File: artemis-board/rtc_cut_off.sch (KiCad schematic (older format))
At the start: 17 parts, among them Q1 2N7002, Q10 AO3401A, Q11 2N7002, Q3 2N7002, U7 PCF8563T, U9 TCA6408A, Y2 32.768KHz

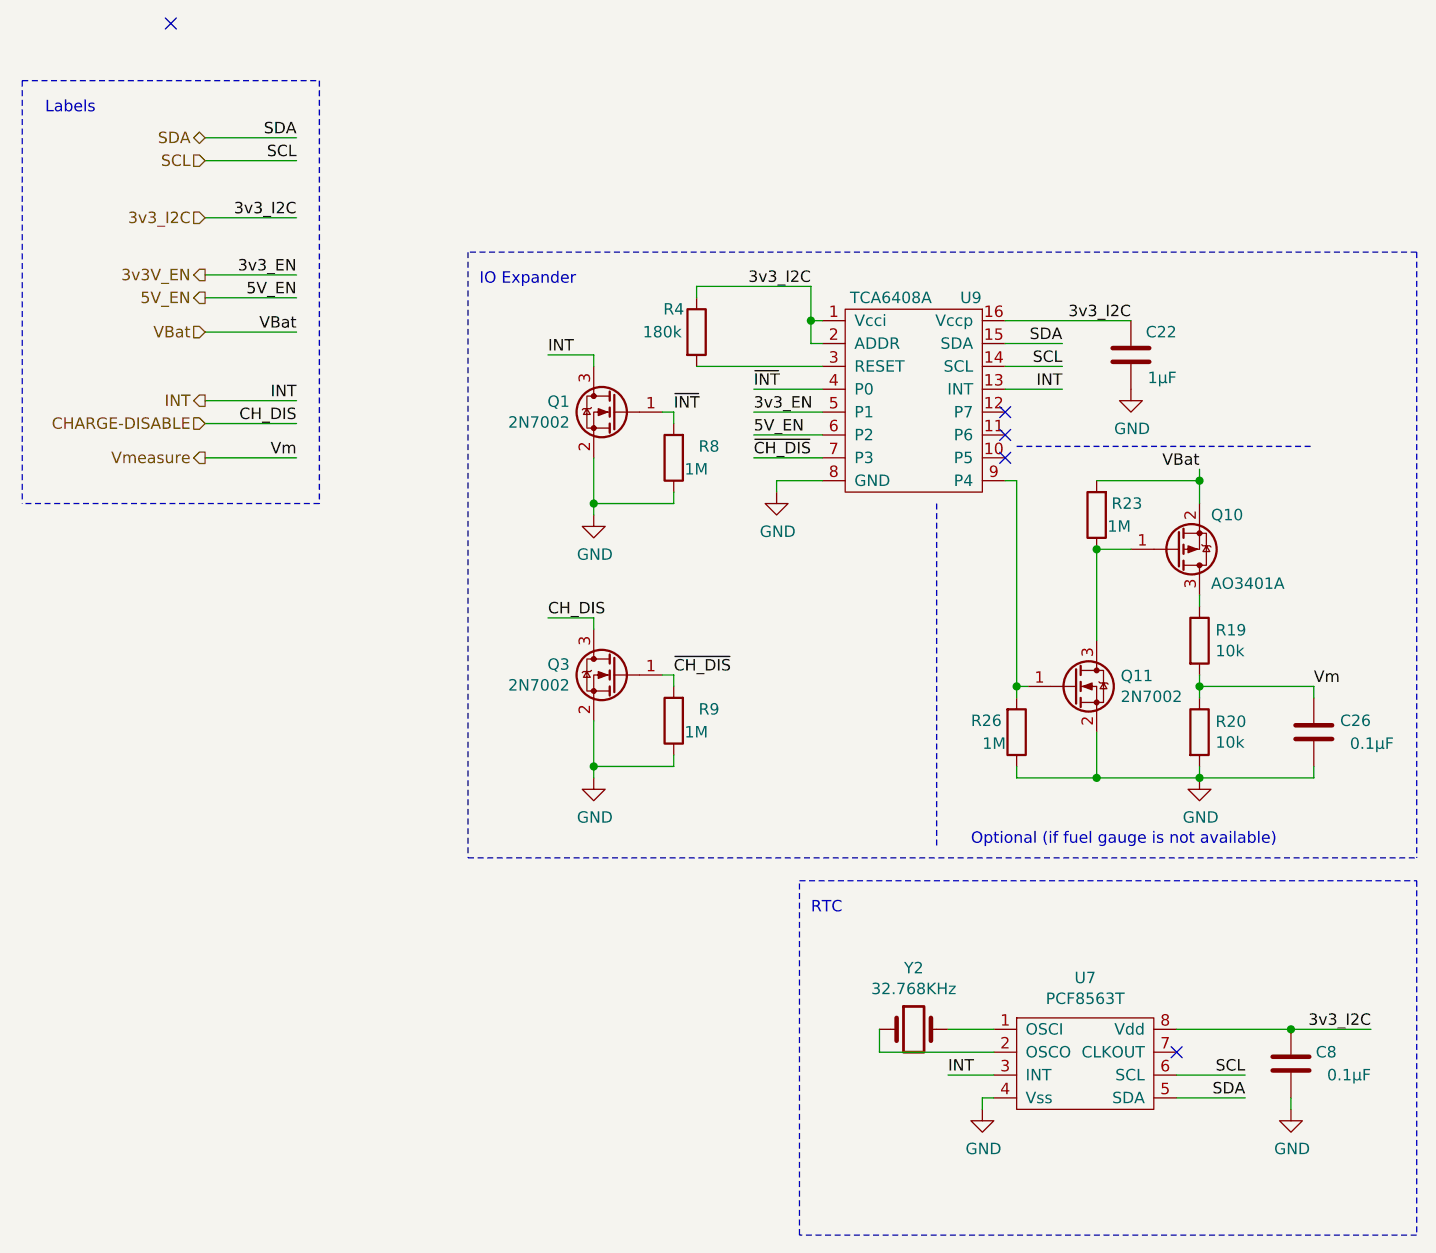
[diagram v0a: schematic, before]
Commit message: added PCA9557 and swapped IO expander for it
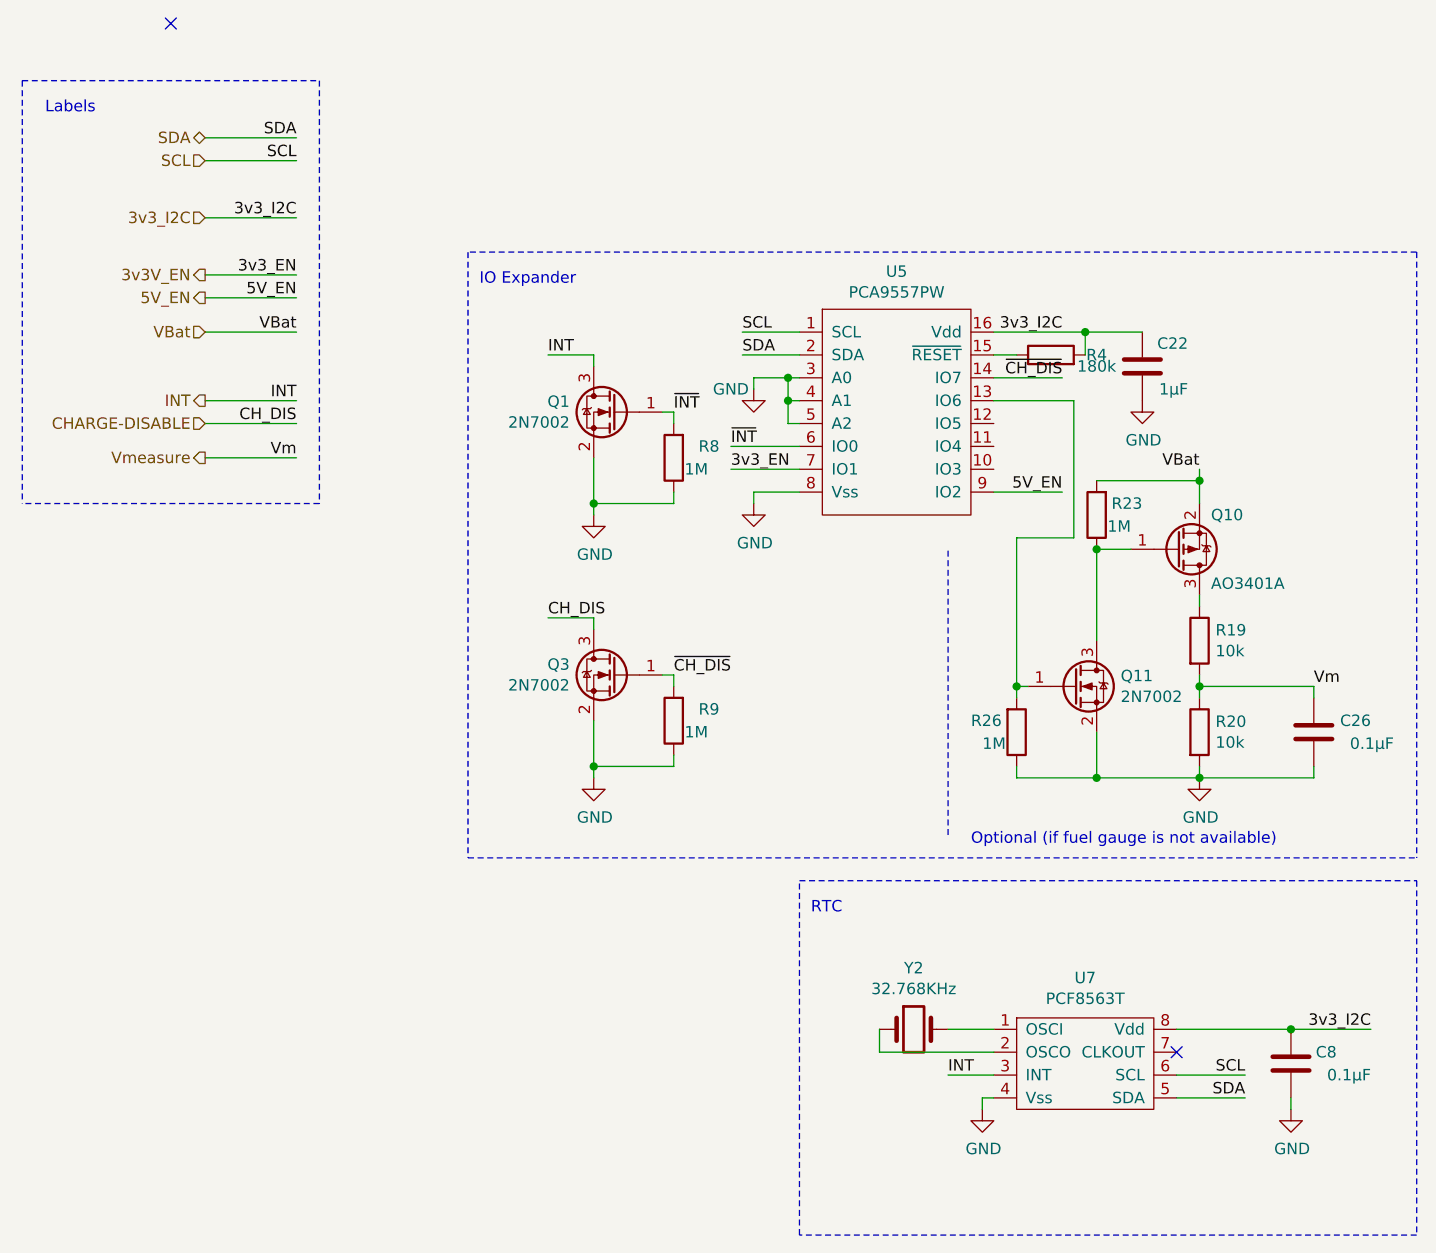
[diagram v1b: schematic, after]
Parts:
- removed U9: TCA6408A, Package_SO:TSSOP-16_4.4x5mm_P0.65mm, symbol TCA6408APWR:TCA6408A
- added U5: PCA9557PW, Package_SO:TSSOP-16_4.4x5mm_P0.65mm, symbol PCA9557:PCA9557PW
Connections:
- net 3v3V_EN: now also U5.7 (IO1)
- net 3v3_I2C: now also R4.2, U5.16 (Vdd); no longer R4.1
- net 5V_EN: now also U5.9 (IO2)
- net GND: now also U5.3 (A0), U5.4 (A1), U5.5 (A2), U5.8 (Vss)
- net SCL: now also U5.1 (SCL)
- net SDA: now also U5.2 (SDA)
- net ~CH_DIS: now also U5.14 (IO7)
- net ~INT: now also U5.6 (IO0)
- net at Q11.1 (G), R26.2: now also U5.13 (IO6)
- new net: R4.1, U5.15 (~RESET)
- no-connect marks 5 -> 2
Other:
- moved on the sheet: C22, R4
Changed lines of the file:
@@
 	4300 4850 4800 4850
 NoConn ~ 5600 4850
-$Comp
-L TCA6408APWR:TCA6408A U9
-U 1 1 5F8103C2
-P 4450 1800
-F 0 "U9" H 4700 2050 50  0000 C CNN
-F 1 "TCA6408A" H 4350 2050 50  0000 C CNN
-F 2 "Package_SO:TSSOP-16_4.4x5mm_P0.65mm" H 4500 2300 50  0001 C CNN
-F 3 "https://www.ti.com/lit/ds/symlink/tca6408a.pdf?ts=1602171918658&ref_url=https%253A%252F%252Fwww.ti.com%252Fproduct%252FTCA6408A" H 4700 2050 50  0001 C CNN
-F 4 "C206177" H 4700 2450 50  0001 C CNN "LCSC"
-	1    4450 1800
-	1    0    0    -1
-$EndComp
 Text HLabel 1350 1200 0    50   Input ~ 0
 3v3_I2C
-Wire Wire Line
-	4050 1650 4000 1650
 $Comp
 L power:GND #PWR0109
@@
 Wire Wire Line
 	2850 1800 3050 1800
-Text Label 5100 1950 2    50   ~ 0
-INT
-Wire Wire Line
-	4850 1950 5100 1950
 Wire Wire Line
 	1350 2000 1750 2000
@@
 Wire Wire Line
 	1350 850  1750 850
-Text Label 5100 1750 2    50   ~ 0
-SDA
-Text Label 5100 1850 2    50   ~ 0
-SCL
-Wire Wire Line
-	4850 1750 5100 1750
-Wire Wire Line
-	4850 1850 5100 1850
 Wire Wire Line
 	6100 4750 6450 4750
@@
 Wire Notes Line
 	1850 2450 550  2450
-Text Label 3750 2050 0    50   ~ 0
+Text Label 3650 2300 0    50   ~ 0
 3v3_EN
-Text Label 3750 2150 0    50   ~ 0
+Text Label 5100 2400 2    50   ~ 0
 5V_EN
-Text Label 3750 2250 0    50   ~ 0
+Text Label 5100 1900 2    50   ~ 0
 ~CH_DIS
-$Comp
-L Device:R R4
-U 1 1 5FC6F3D4
-P 3500 1700
-F 0 "R4" H 3400 1800 50  0000 C CNN
-F 1 "180k" H 3350 1700 50  0000 C CNN
-F 2 "Resistor_SMD:R_0603_1608Metric_Pad1.05x0.95mm_HandSolder" V 3430 1700 50  0001 C CNN
-F 3 "~" H 3500 1700 50  0001 C CNN
-F 4 "C22827" H 3500 1700 50  0001 C CNN "LCSC"
-	1    3500 1700
-	1    0    0    -1
-$EndComp
-Wire Wire Line
-	4000 1500 4000 1650
-Text Label 4000 1500 2    50   ~ 0
+Text Label 5100 1700 2    50   ~ 0
 3v3_I2C
 Wire Wire Line
@@
 L Device:C C22
 U 1 1 5FC9C8EC
-P 5400 1800
-F 0 "C22" H 5200 1700 50  0000 L CNN
-F 1 "1µF" H 5200 1900 50  0000 L CNN
-F 2 "Capacitor_SMD:C_0603_1608Metric_Pad1.08x0.95mm_HandSolder" H 5438 1650 50  0001 C CNN
-F 3 "~" H 5400 1800 50  0001 C CNN
-F 4 "C15849" H 5400 1800 50  0001 C CNN "LCSC"
-	1    5400 1800
+P 5450 1850
+F 0 "C22" H 5250 1750 50  0000 L CNN
+F 1 "1µF" H 5250 1950 50  0000 L CNN
+F 2 "Capacitor_SMD:C_0603_1608Metric_Pad1.08x0.95mm_HandSolder" H 5488 1700 50  0001 C CNN
+F 3 "~" H 5450 1850 50  0001 C CNN
+F 4 "C15849" H 5450 1850 50  0001 C CNN "LCSC"
+	1    5450 1850
 	-1   0    0    1
 $EndComp
-Wire Wire Line
-	4850 1650 5400 1650
 $Comp
 L power:GND #PWR0110
 U 1 1 5FCA03ED
-P 5400 1950
-F 0 "#PWR0110" H 5400 1700 50  0001 C CNN
-F 1 "GND" H 5405 1777 50  0000 C CNN
-F 2 "" H 5400 1950 50  0001 C CNN
-F 3 "" H 5400 1950 50  0001 C CNN
-	1    5400 1950
+P 5450 2000
+F 0 "#PWR0110" H 5450 1750 50  0001 C CNN
+F 1 "GND" H 5455 1827 50  0000 C CNN
+F 2 "" H 5450 2000 50  0001 C CNN
+F 3 "" H 5450 2000 50  0001 C CNN
+	1    5450 2000
 	1    0    0    -1
 $EndComp
@@
 3v3_I2C
 Wire Wire Line
-	3750 2050 4050 2050
-Wire Wire Line
-	4050 2150 3750 2150
-Wire Wire Line
-	3750 2250 4050 2250
-NoConn ~ 4850 2250
-NoConn ~ 4850 2150
-NoConn ~ 4850 2050
-Wire Wire Line
-	3500 1850 4050 1850
+	3950 2300 3650 2300
+Wire Wire Line
+	4800 2400 5100 2400
+Wire Wire Line
+	5100 1900 4800 1900
 Text HLabel 1350 1700 0    50   Input ~ 0
 VBat
@@
 Wire Wire Line
 	1750 1700 1350 1700
-Wire Wire Line
-	3500 1550 3500 1500
-Wire Wire Line
-	4050 1750 4000 1750
-Wire Wire Line
-	4000 1750 4000 1650
-Connection ~ 4000 1650
-Text Label 3750 1950 0    50   ~ 0
+Text Label 3650 2200 0    50   ~ 0
 ~INT
 Wire Wire Line
-	3750 1950 4050 1950
-Wire Wire Line
-	4050 2350 3850 2350
-Wire Wire Line
-	3850 2350 3850 2400
+	3650 2200 3950 2200
+Wire Wire Line
+	3950 2400 3750 2400
+Wire Wire Line
+	3750 2400 3750 2450
 $Comp
 L power:GND #PWR0111
 U 1 1 60A0ABA2
-P 3850 2400
-F 0 "#PWR0111" H 3850 2150 50  0001 C CNN
-F 1 "GND" H 3855 2227 50  0000 C CNN
-F 2 "" H 3850 2400 50  0001 C CNN
-F 3 "" H 3850 2400 50  0001 C CNN
-	1    3850 2400
+P 3750 2450
+F 0 "#PWR0111" H 3750 2200 50  0001 C CNN
+F 1 "GND" H 3755 2277 50  0000 C CNN
+F 2 "" H 3750 2450 50  0001 C CNN
+F 3 "" H 3750 2450 50  0001 C CNN
+	1    3750 2450
 	1    0    0    -1
 $EndComp
@@
 Text Notes 4700 3950 0    50   ~ 0
 Optional (if fuel gauge is not available)
-Wire Notes Line
-	4550 2450 4550 3950
-Wire Notes Line
-	4900 2200 6200 2200
 Connection ~ 5700 2350
 Wire Wire Line
@@
 Wire Wire Line
 	6200 3650 5700 3650
-Wire Wire Line
-	4900 3250 4900 2350
-Wire Wire Line
-	4900 2350 4850 2350
+Wire Notes Line
+	6650 1350 2500 1350
+Wire Notes Line
+	2500 4000 6650 4000
+Wire Notes Line
+	2500 1350 2500 4000
+$Comp
+L PCA9557:PCA9557PW U5
+U 1 1 60F0D833
+P 4400 1450
+F 0 "U5" H 4375 1465 50  0000 C CNN
+F 1 "PCA9557PW" H 4375 1374 50  0000 C CNN
+F 2 "Package_SO:TSSOP-16_4.4x5mm_P0.65mm" H 4400 1450 50  0001 C CNN
+F 3 "" H 4400 1450 50  0001 C CNN
+F 4 "C141380" H 4400 1450 50  0001 C CNN "LCSC"
+	1    4400 1450
+	1    0    0    -1
+$EndComp
+Text Label 3700 1800 0    50   ~ 0
+SDA
+Text Label 3700 1700 0    50   ~ 0
+SCL
+Wire Wire Line
+	3950 1800 3700 1800
+Wire Wire Line
+	3950 1700 3700 1700
+$Comp
+L Device:R R4
+U 1 1 5FC6F3D4
+P 5050 1800
+F 0 "R4" V 5050 1600 50  0000 C CNN
+F 1 "180k" V 5000 1600 50  0000 C CNN
+F 2 "Resistor_SMD:R_0603_1608Metric_Pad1.05x0.95mm_HandSolder" V 4980 1800 50  0001 C CNN
+F 3 "~" H 5050 1800 50  0001 C CNN
+F 4 "C22827" H 5050 1800 50  0001 C CNN "LCSC"
+	1    5050 1800
+	0    -1   -1   0
+$EndComp
+Wire Wire Line
+	4800 1800 4900 1800
+Wire Wire Line
+	5200 1700 5200 1800
+Wire Wire Line
+	4800 1700 5200 1700
+Wire Wire Line
+	5450 1700 5200 1700
+Connection ~ 5200 1700
+Wire Notes Line
+	4600 3900 4600 2650
+Wire Wire Line
+	4900 3250 4900 2600
+Wire Wire Line
+	4900 2600 5150 2600
 Connection ~ 4900 3250
-Wire Notes Line
-	6650 1350 2500 1350
-Wire Notes Line
-	2500 4000 6650 4000
-Wire Notes Line
-	2500 1350 2500 4000
-Text Label 5400 1650 2    50   ~ 0
-3v3_I2C
-Wire Wire Line
-	4000 1500 3500 1500
+Wire Wire Line
+	3950 2100 3900 2100
+Wire Wire Line
+	3900 2100 3900 2000
+Wire Wire Line
+	3900 2000 3950 2000
+Wire Wire Line
+	3900 2000 3900 1900
+Wire Wire Line
+	3900 1900 3950 1900
+Connection ~ 3900 2000
+Wire Wire Line
+	3750 1900 3750 1950
+$Comp
+L power:GND #PWR0118
+U 1 1 60F58134
+P 3750 1950
+F 0 "#PWR0118" H 3750 1700 50  0001 C CNN
+F 1 "GND" H 3650 1950 50  0000 C CNN
+F 2 "" H 3750 1950 50  0001 C CNN
+F 3 "" H 3750 1950 50  0001 C CNN
+	1    3750 1950
+	1    0    0    -1
+$EndComp
+Wire Wire Line
+	3750 1900 3900 1900
+Connection ~ 3900 1900
+Wire Wire Line
+	4800 2000 5150 2000
+Wire Wire Line
+	5150 2000 5150 2600
 $EndSCHEMATC

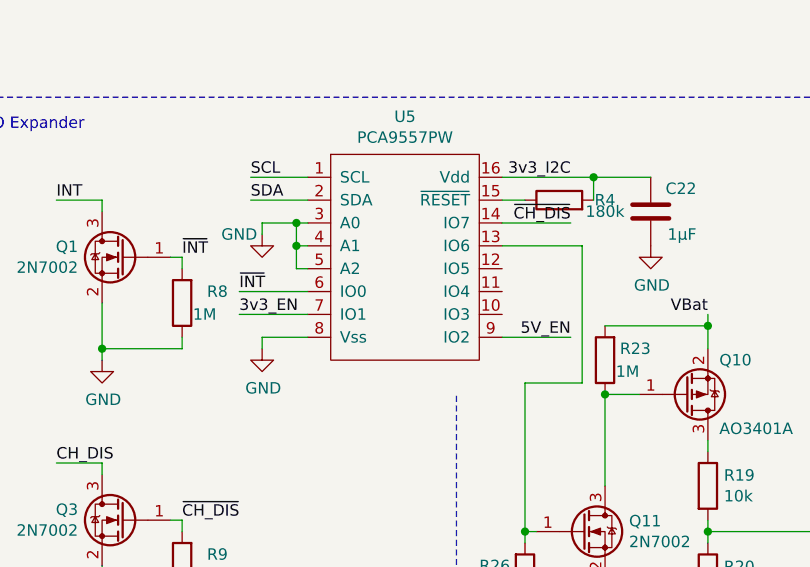
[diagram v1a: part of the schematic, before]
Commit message: added datasheet for pca9557 and connected ~INT to another pin
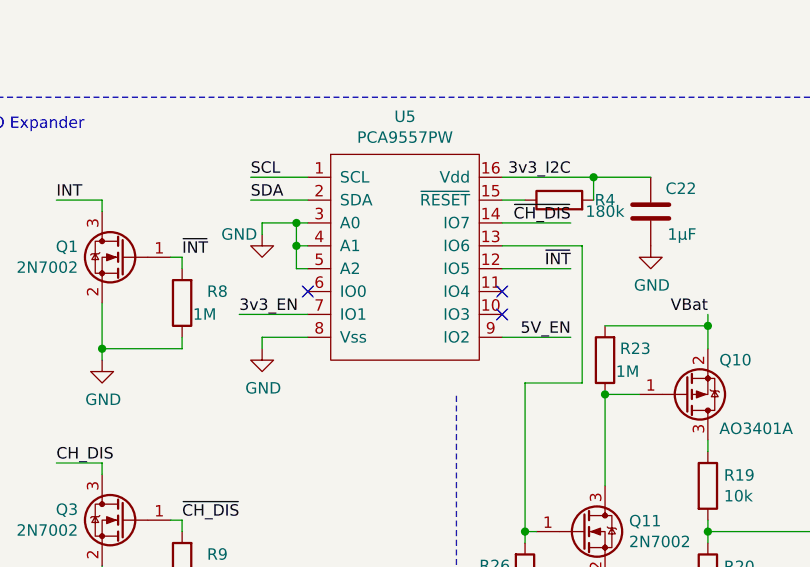
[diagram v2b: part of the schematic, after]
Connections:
- net ~INT: now also U5.12 (IO5); no longer U5.6 (IO0)
- no-connect marks 2 -> 5
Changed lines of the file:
@@
 Wire Wire Line
 	1750 1700 1350 1700
-Text Label 3650 2200 0    50   ~ 0
+Text Label 5100 2100 2    50   ~ 0
 ~INT
 Wire Wire Line
-	3650 2200 3950 2200
+	5100 2100 4800 2100
 Wire Wire Line
 	3950 2400 3750 2400
@@
 F 1 "PCA9557PW" H 4375 1374 50  0000 C CNN
 F 2 "Package_SO:TSSOP-16_4.4x5mm_P0.65mm" H 4400 1450 50  0001 C CNN
-F 3 "" H 4400 1450 50  0001 C CNN
+F 3 "https://www.ti.com/lit/ds/symlink/pca9557.pdf?ts=1627895395764" H 4400 1450 50  0001 C CNN
 F 4 "C141380" H 4400 1450 50  0001 C CNN "LCSC"
 	1    4400 1450
@@
 Wire Wire Line
 	5150 2000 5150 2600
+NoConn ~ 3950 2200
+NoConn ~ 4800 2200
+NoConn ~ 4800 2300
 $EndSCHEMATC

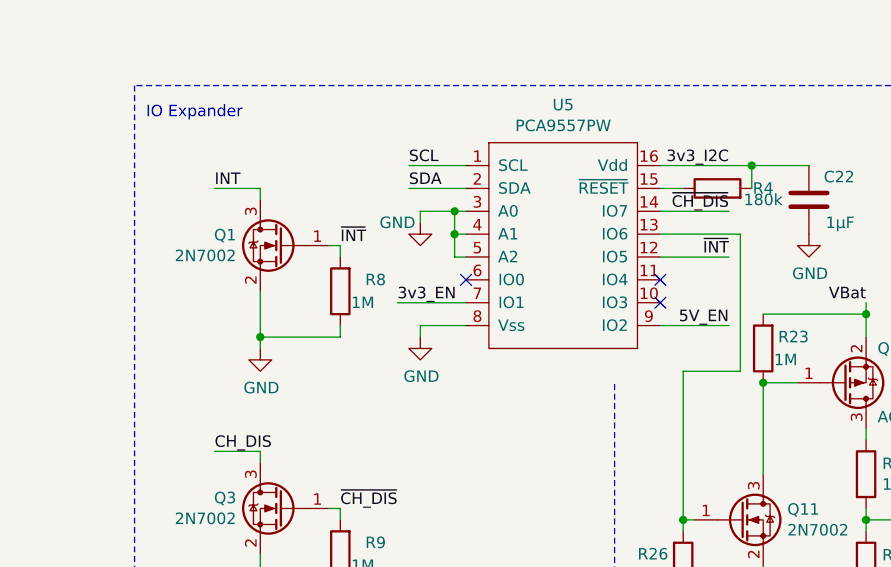
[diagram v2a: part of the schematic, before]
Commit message: alternative package for PCA9557 and smaller silk
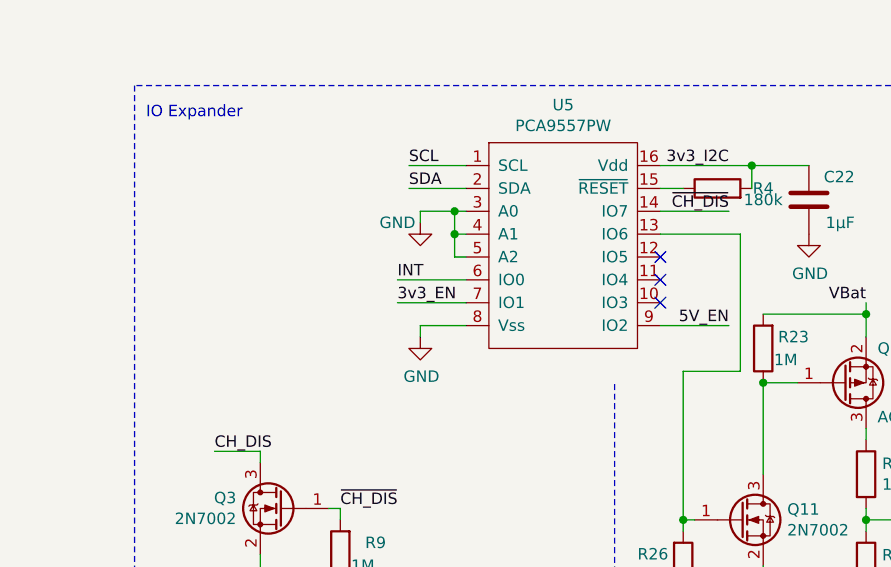
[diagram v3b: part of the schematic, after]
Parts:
- removed Q1: 2N7002, Package_TO_SOT_SMD:SOT-23, symbol Transistor_FET:2N7002
- removed R8: 1M, Resistor_SMD:R_0603_1608Metric_Pad0.98x0.95mm_HandSolder, symbol Device:R
- U5: footprint Package_SO:TSSOP-16_4.4x5mm_P0.65mm -> Package_SO:SOP-16_3.9x9.9mm_P1.27mm
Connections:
- net INT: now also U5.6 (IO0)
- net ~INT: no longer names the net of U5.12 (IO5)
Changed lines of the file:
@@
 Text HLabel 1350 1200 0    50   Input ~ 0
 3v3_I2C
-$Comp
-L power:GND #PWR0109
-U 1 1 5F81AC3F
-P 3050 2500
-F 0 "#PWR0109" H 3050 2250 50  0001 C CNN
-F 1 "GND" H 3055 2327 50  0000 C CNN
-F 2 "" H 3050 2500 50  0001 C CNN
-F 3 "" H 3050 2500 50  0001 C CNN
-	1    3050 2500
-	1    0    0    -1
-$EndComp
-$Comp
-L Transistor_FET:2N7002 Q1
-U 1 1 5F81E351
-P 3150 2050
-F 0 "Q1" H 3355 2096 50  0000 L CNN
-F 1 "2N7002" H 3355 2005 50  0000 L CNN
-F 2 "Package_TO_SOT_SMD:SOT-23" H 3350 1975 50  0001 L CIN
-F 3 "https://www.fairchildsemi.com/datasheets/2N/2N7002.pdf" H 3150 2050 50  0001 L CNN
-F 4 "C8545" H 3150 2050 50  0001 C CNN "LCSC"
-	1    3150 2050
-	-1   0    0    -1
-$EndComp
-Wire Wire Line
-	3050 1800 3050 1850
 Text HLabel 1350 950  0    50   Input ~ 0
 SCL
@@
 Wire Wire Line
 	4600 4950 4800 4950
-Text Label 2850 1800 0    50   ~ 0
+Text Label 3650 2200 0    50   ~ 0
 INT
-Wire Wire Line
-	2850 1800 3050 1800
 Wire Wire Line
 	1350 2000 1750 2000
@@
 Text Label 5100 1700 2    50   ~ 0
 3v3_I2C
-Wire Wire Line
-	3350 2050 3400 2050
 $Comp
 L Device:C C22
@@
 Wire Wire Line
 	1750 1700 1350 1700
-Text Label 5100 2100 2    50   ~ 0
-~INT
-Wire Wire Line
-	5100 2100 4800 2100
 Wire Wire Line
 	3950 2400 3750 2400
@@
 Wire Notes Line
 	6650 1350 6650 4000
-Text Label 3400 2050 0    50   ~ 0
-~INT
 $Comp
 L power:GND #PWR0115
@@
 Text Label 1750 2250 2    50   ~ 0
 Vm
-Wire Wire Line
-	3400 2100 3400 2050
-Wire Wire Line
-	3400 2400 3400 2450
-$Comp
-L Device:R R?
-U 1 1 60A05ACF
-P 3400 2250
-AR Path="/5F639F48/60A05ACF" Ref="R?"  Part="1"
-AR Path="/5F63A0E9/60A05ACF" Ref="R?"  Part="1"
-AR Path="/5F63A00B/60A05ACF" Ref="R8"  Part="1"
-F 0 "R8" H 3200 2200 50  0000 L CNN
-F 1 "1M" H 3250 2300 50  0000 L CNN
-F 2 "Resistor_SMD:R_0603_1608Metric_Pad0.98x0.95mm_HandSolder" V 3330 2250 50  0001 C CNN
-F 3 "~" H 3400 2250 50  0001 C CNN
-F 4 "C22935" H 3400 2250 50  0001 C CNN "LCSC"
-	1    3400 2250
-	-1   0    0    1
-$EndComp
-Wire Wire Line
-	3050 2250 3050 2450
-Wire Wire Line
-	3050 2450 3050 2500
-Connection ~ 3050 2450
-Wire Wire Line
-	3050 2450 3400 2450
 Wire Wire Line
 	3400 3250 3400 3200
@@
 F 0 "U5" H 4375 1465 50  0000 C CNN
 F 1 "PCA9557PW" H 4375 1374 50  0000 C CNN
-F 2 "Package_SO:TSSOP-16_4.4x5mm_P0.65mm" H 4400 1450 50  0001 C CNN
+F 2 "Package_SO:SOP-16_3.9x9.9mm_P1.27mm" H 4400 1450 50  0001 C CNN
 F 3 "https://www.ti.com/lit/ds/symlink/pca9557.pdf?ts=1627895395764" H 4400 1450 50  0001 C CNN
 F 4 "C141380" H 4400 1450 50  0001 C CNN "LCSC"
@@
 Wire Wire Line
 	5150 2000 5150 2600
-NoConn ~ 3950 2200
 NoConn ~ 4800 2200
 NoConn ~ 4800 2300
+Wire Wire Line
+	3950 2200 3650 2200
+NoConn ~ 4800 2100
 $EndSCHEMATC
